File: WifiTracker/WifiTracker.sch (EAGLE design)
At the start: 23 parts, among them Y1 16MHz

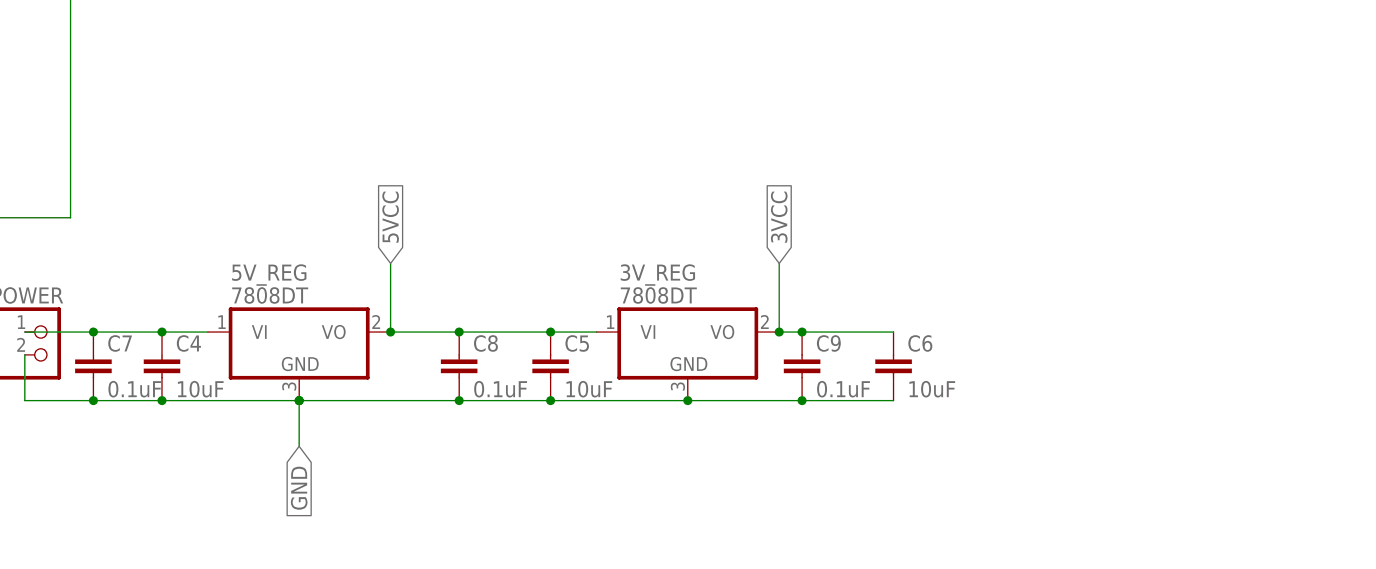
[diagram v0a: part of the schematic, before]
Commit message: Change generic voltage regulator with specific one
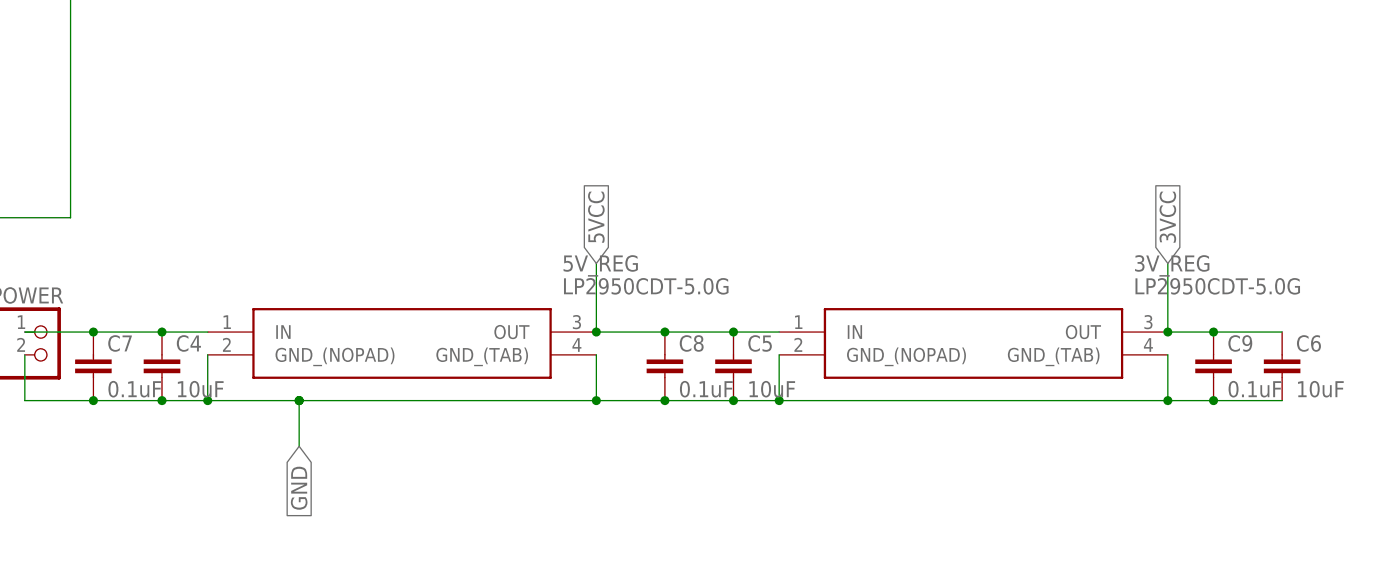
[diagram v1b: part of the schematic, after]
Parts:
- 3V_REG, 5V_REG: value 7808DT -> LP2950CDT-5.0G; device linear:7808DT -> LP2950CDT-5.0G:LP2950CDT-5.0G
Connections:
- net 3VCC: now also 3V_REG.OUT; no longer 3V_REG.VO
- net 5VCC: now also 3V_REG.IN, 5V_REG.OUT; no longer 3V_REG.VI, 5V_REG.VO
- net GND: now also 3V_REG.GND_(NOPAD), 3V_REG.GND_(TAB), 5V_REG.GND_(NOPAD), 5V_REG.GND_(TAB); no longer 3V_REG.GND, 5V_REG.GND
- net VIN: now also 5V_REG.IN; no longer 5V_REG.VI
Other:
- moved on the sheet: C5, C6, C8, C9

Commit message: Added 5v to 3.3V regulators to Wifitrackers
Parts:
- added Q1, Q2: BSS123, transistor-small-signal:BSS123
- added R10, R7, R8, R9: 10kΩ, eagle-ltspice:RR1210
- R1, R2: value 10KOHM -> 10KΩ
- R3, R5, R6: value 10KOHM -> 10kΩ
- R4: value 1MOHM -> 1MΩ
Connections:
- new net N$1: WIFI_PRO.TXD
- new net N$2: WIFI_STA.RXD
- new net N$3: Q1.S, R7.2, WIFI_PRO.RXD
- new net N$4: Q2.S, R9.2
- new net PRO_RXD1: Q2.D, R10.2
- net 3VCC: now also Q1.G, Q2.G, R7.1, R9.1
- net 5VCC: now also R10.1, R8.1
- net GND: no longer WIFI_PRO.GPIO2, WIFI_STA.GPIO2
- net PRO_RXD: now also Q1.D, R8.2; no longer WIFI_PRO.RXD
- net PRO_TXD: no longer WIFI_PRO.TXD
- net STA_RXD: no longer WIFI_STA.RXD
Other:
- note added: "DMG3420U"
- moved on the sheet: R1, R2, WIFI_STA

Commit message: Changed 3.3V regulator
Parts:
- removed 3V_REG: LP2950CDT-5.0G, LP2950CDT-5.0G:LP2950CDT-5.0G
- added IC1: TS1117CP33-R0, TS1117CP33-R0:TS1117CP33-R0
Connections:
- net 3VCC: now also IC1.OUT, IC1.OUT_(TAB); no longer 3V_REG.OUT
- net 5VCC: now also IC1.IN; no longer 3V_REG.IN
- net GND: now also IC1.GND; no longer 3V_REG.GND_(NOPAD), 3V_REG.GND_(TAB)
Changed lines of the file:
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@@
 <part name="R5" library="eagle-ltspice" library_urn="urn:adsk.eagle:library:217" deviceset="R" device="R1210" package3d_urn="urn:adsk.eagle:package:13299/1" value="10kΩ"/>
 <part name="5V_REG" library="LP2950CDT-5.0G" deviceset="LP2950CDT-5.0G" device=""/>
-<part name="3V_REG" library="LP2950CDT-5.0G" deviceset="LP2950CDT-5.0G" device=""/>
 <part name="R7" library="eagle-ltspice" library_urn="urn:adsk.eagle:library:217" deviceset="R" device="R1210" package3d_urn="urn:adsk.eagle:package:13299/1" value="10kΩ"/>
 <part name="Q1" library="transistor-small-signal" library_urn="urn:adsk.eagle:library:401" deviceset="BSS123" device="" package3d_urn="urn:adsk.eagle:package:29752/1"/>
@@
 <part name="Q2" library="transistor-small-signal" library_urn="urn:adsk.eagle:library:401" deviceset="BSS123" device="" package3d_urn="urn:adsk.eagle:package:29752/1"/>
 <part name="R10" library="eagle-ltspice" library_urn="urn:adsk.eagle:library:217" deviceset="R" device="R1210" package3d_urn="urn:adsk.eagle:package:13299/1" value="10kΩ"/>
+<part name="IC1" library="TS1117CP33-R0" deviceset="TS1117CP33-R0" device=""/>
 </parts>
 <sheets>
@@
 <attribute name="VALUE" x="153.67" y="17.78" size="1.778" layer="96" align="center-left"/>
 </instance>
-<instance part="3V_REG" gate="G$1" x="177.8" y="12.7" smashed="yes">
-<attribute name="NAME" x="217.17" y="20.32" size="1.778" layer="95" align="center-left"/>
-<attribute name="VALUE" x="217.17" y="17.78" size="1.778" layer="96" align="center-left"/>
-</instance>
 <instance part="R7" gate="G$1" x="66.04" y="55.88" smashed="yes" rot="R180">
 <attribute name="NAME" x="69.85" y="54.3814" size="1.778" layer="95" rot="R180"/>
@@
 <attribute name="VALUE" x="14.478" y="69.85" size="1.778" layer="96" rot="R270"/>
 </instance>
+<instance part="IC1" gate="G$1" x="177.8" y="12.7"/>
 </instances>
 <busses>
@@
 <wire x1="165.1" y1="5.08" x2="172.72" y2="5.08" width="0.1524" layer="91"/>
 <wire x1="172.72" y1="5.08" x2="177.8" y2="5.08" width="0.1524" layer="91"/>
-<wire x1="177.8" y1="5.08" x2="220.98" y2="5.08" width="0.1524" layer="91"/>
-<wire x1="220.98" y1="5.08" x2="226.06" y2="5.08" width="0.1524" layer="91"/>
+<wire x1="177.8" y1="5.08" x2="226.06" y2="5.08" width="0.1524" layer="91"/>
 <wire x1="124.46" y1="5.08" x2="124.46" y2="0" width="0.1524" layer="91"/>
 <junction x="124.46" y="5.08"/>
@@
 <wire x1="157.48" y1="10.16" x2="157.48" y2="5.08" width="0.1524" layer="91"/>
 <junction x="157.48" y="5.08"/>
-<pinref part="3V_REG" gate="G$1" pin="GND_(NOPAD)"/>
 <wire x1="177.8" y1="10.16" x2="177.8" y2="5.08" width="0.1524" layer="91"/>
 <junction x="177.8" y="5.08"/>
-<pinref part="3V_REG" gate="G$1" pin="GND_(TAB)"/>
-<wire x1="220.98" y1="10.16" x2="220.98" y2="5.08" width="0.1524" layer="91"/>
-<junction x="220.98" y="5.08"/>
+<pinref part="IC1" gate="G$1" pin="GND"/>
 </segment>
 </net>
@@
 <wire x1="220.98" y1="12.7" x2="220.98" y2="20.32" width="0.1524" layer="91"/>
 <label x="220.98" y="20.32" size="1.778" layer="95" rot="R90" xref="yes"/>
-<pinref part="3V_REG" gate="G$1" pin="OUT"/>
+<pinref part="IC1" gate="G$1" pin="OUT"/>
 <junction x="220.98" y="12.7"/>
+<pinref part="IC1" gate="G$1" pin="OUT_(TAB)"/>
+<wire x1="220.98" y1="10.16" x2="220.98" y2="12.7" width="0.1524" layer="91"/>
 </segment>
 <segment>
@@
 <pinref part="5V_REG" gate="G$1" pin="OUT"/>
 <junction x="157.48" y="12.7"/>
-<pinref part="3V_REG" gate="G$1" pin="IN"/>
 <wire x1="177.8" y1="12.7" x2="172.72" y2="12.7" width="0.1524" layer="91"/>
 <junction x="172.72" y="12.7"/>
+<pinref part="IC1" gate="G$1" pin="IN"/>
 </segment>
 <segment>
@@
 </segment>
 </net>
-<net name="VIN" class="0">
+<net name="VIN" class="1">
 <segment>
 <pinref part="POWER" gate="G$1" pin="1"/>

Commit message: Prepare to print
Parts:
- removed Q1, Q2: BSS123, transistor-small-signal:BSS123
- R10, R8: value 10kΩ -> 2.2kΩ
- R7, R9: value 10kΩ -> 1kΩ
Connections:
- removed net N$1: WIFI_PRO.TXD
- removed net N$2: WIFI_STA.RXD
- removed net N$3: Q1.S, R7.2, WIFI_PRO.RXD
- removed net N$4: Q2.S, R9.2
- removed net PRO_RXD1: Q2.D, R10.2
- new net AT_STXD: ATMEGA.PD3(INT1), R7.1
- new net AT_TXD: ATMEGA.PD1(TXD), R9.1
- net 3VCC: no longer Q1.G, Q2.G, R7.1, R9.1
- net 5VCC: no longer R10.1, R8.1
- net GND: now also R10.2, R8.2
- net PRO_RXD: now also R7.2, R8.1, WIFI_PRO.RXD; no longer ATMEGA.PD3(INT1), Q1.D, R8.2
- net PRO_TXD: now also WIFI_PRO.TXD
- net STA_RXD: now also R10.1, R9.2, WIFI_STA.RXD; no longer ATMEGA.PD1(TXD)
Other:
- note removed: "DMG3420U"
- moved on the sheet: R10, R7, R8, R9
